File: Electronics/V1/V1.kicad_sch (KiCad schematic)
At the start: 2 parts, among them U1 ADPD144RI, U3 XIAO-ESP32-C3

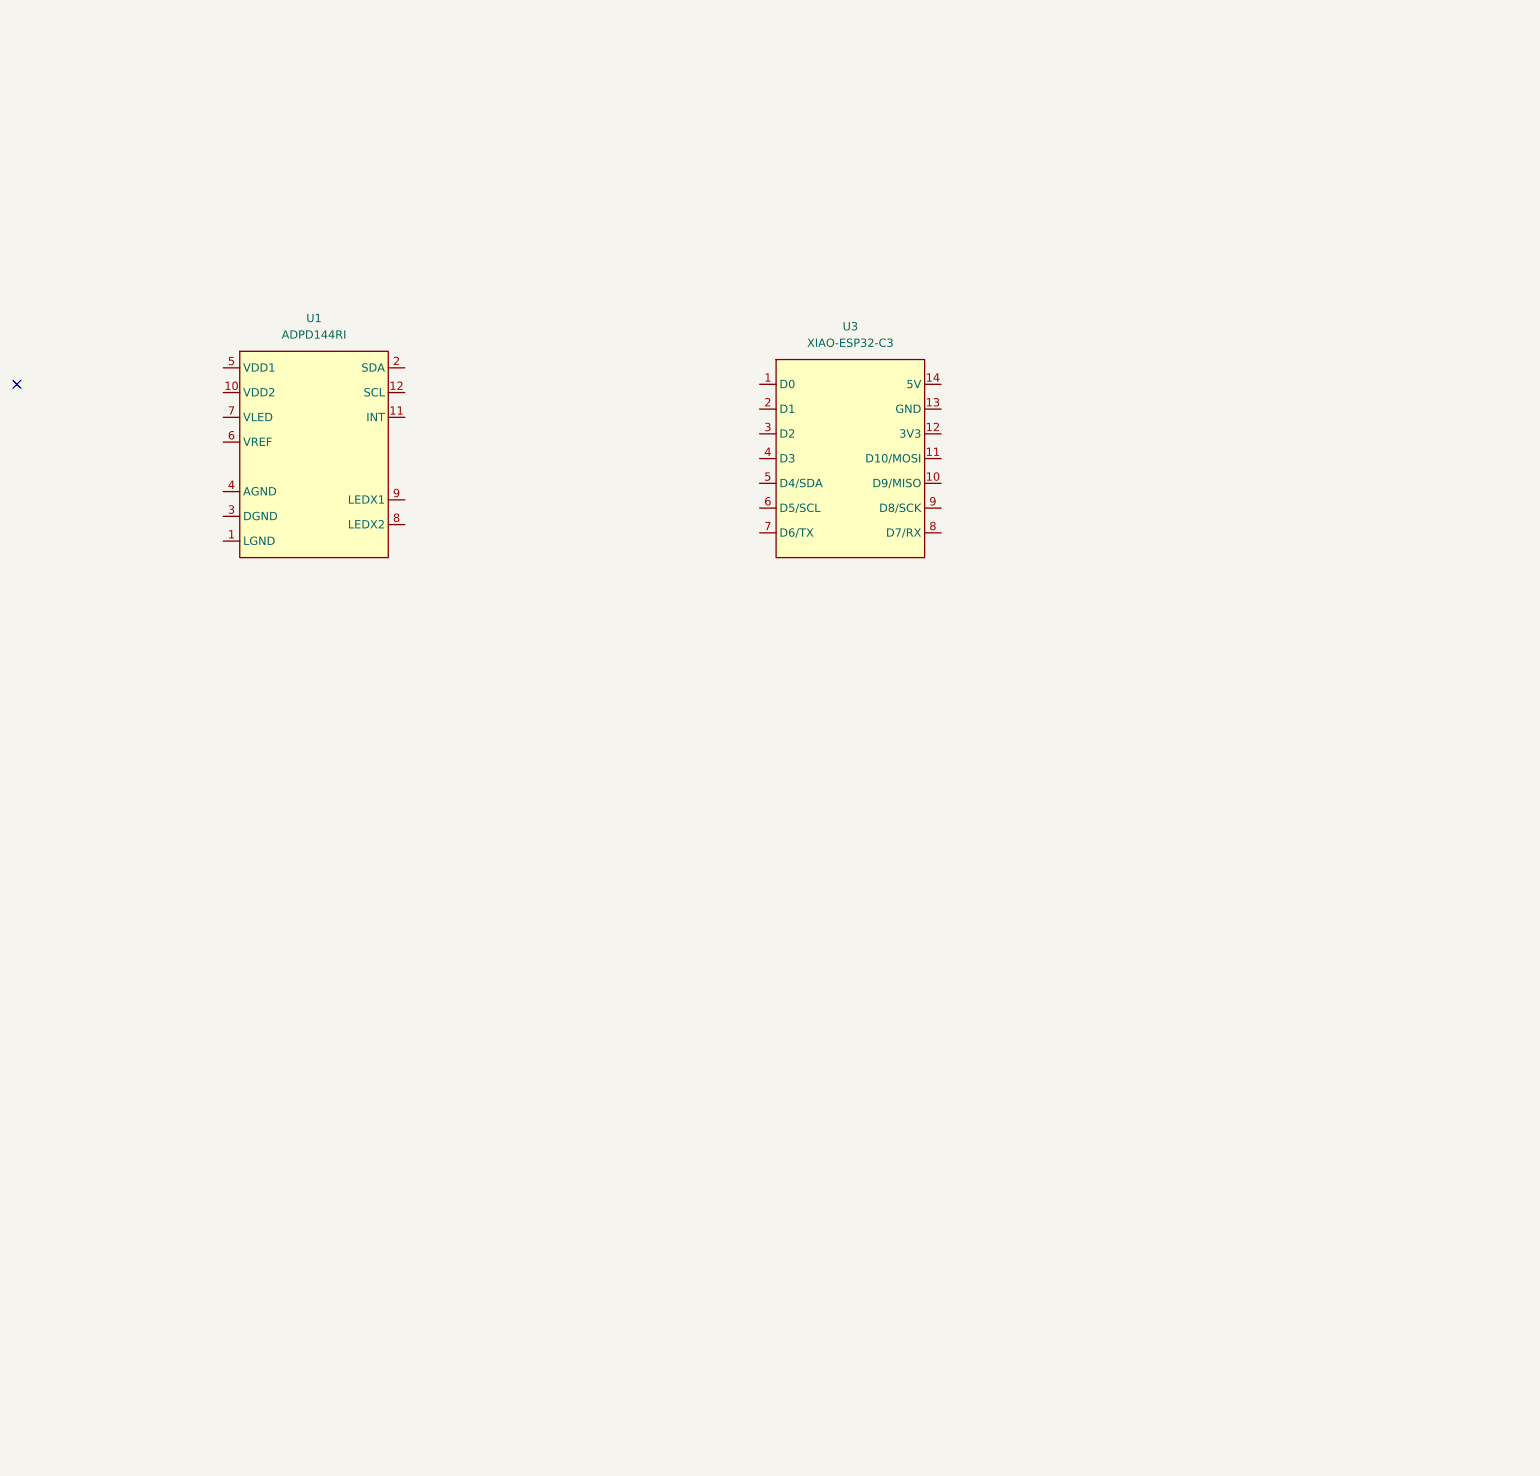
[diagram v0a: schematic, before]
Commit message: Added more symbols
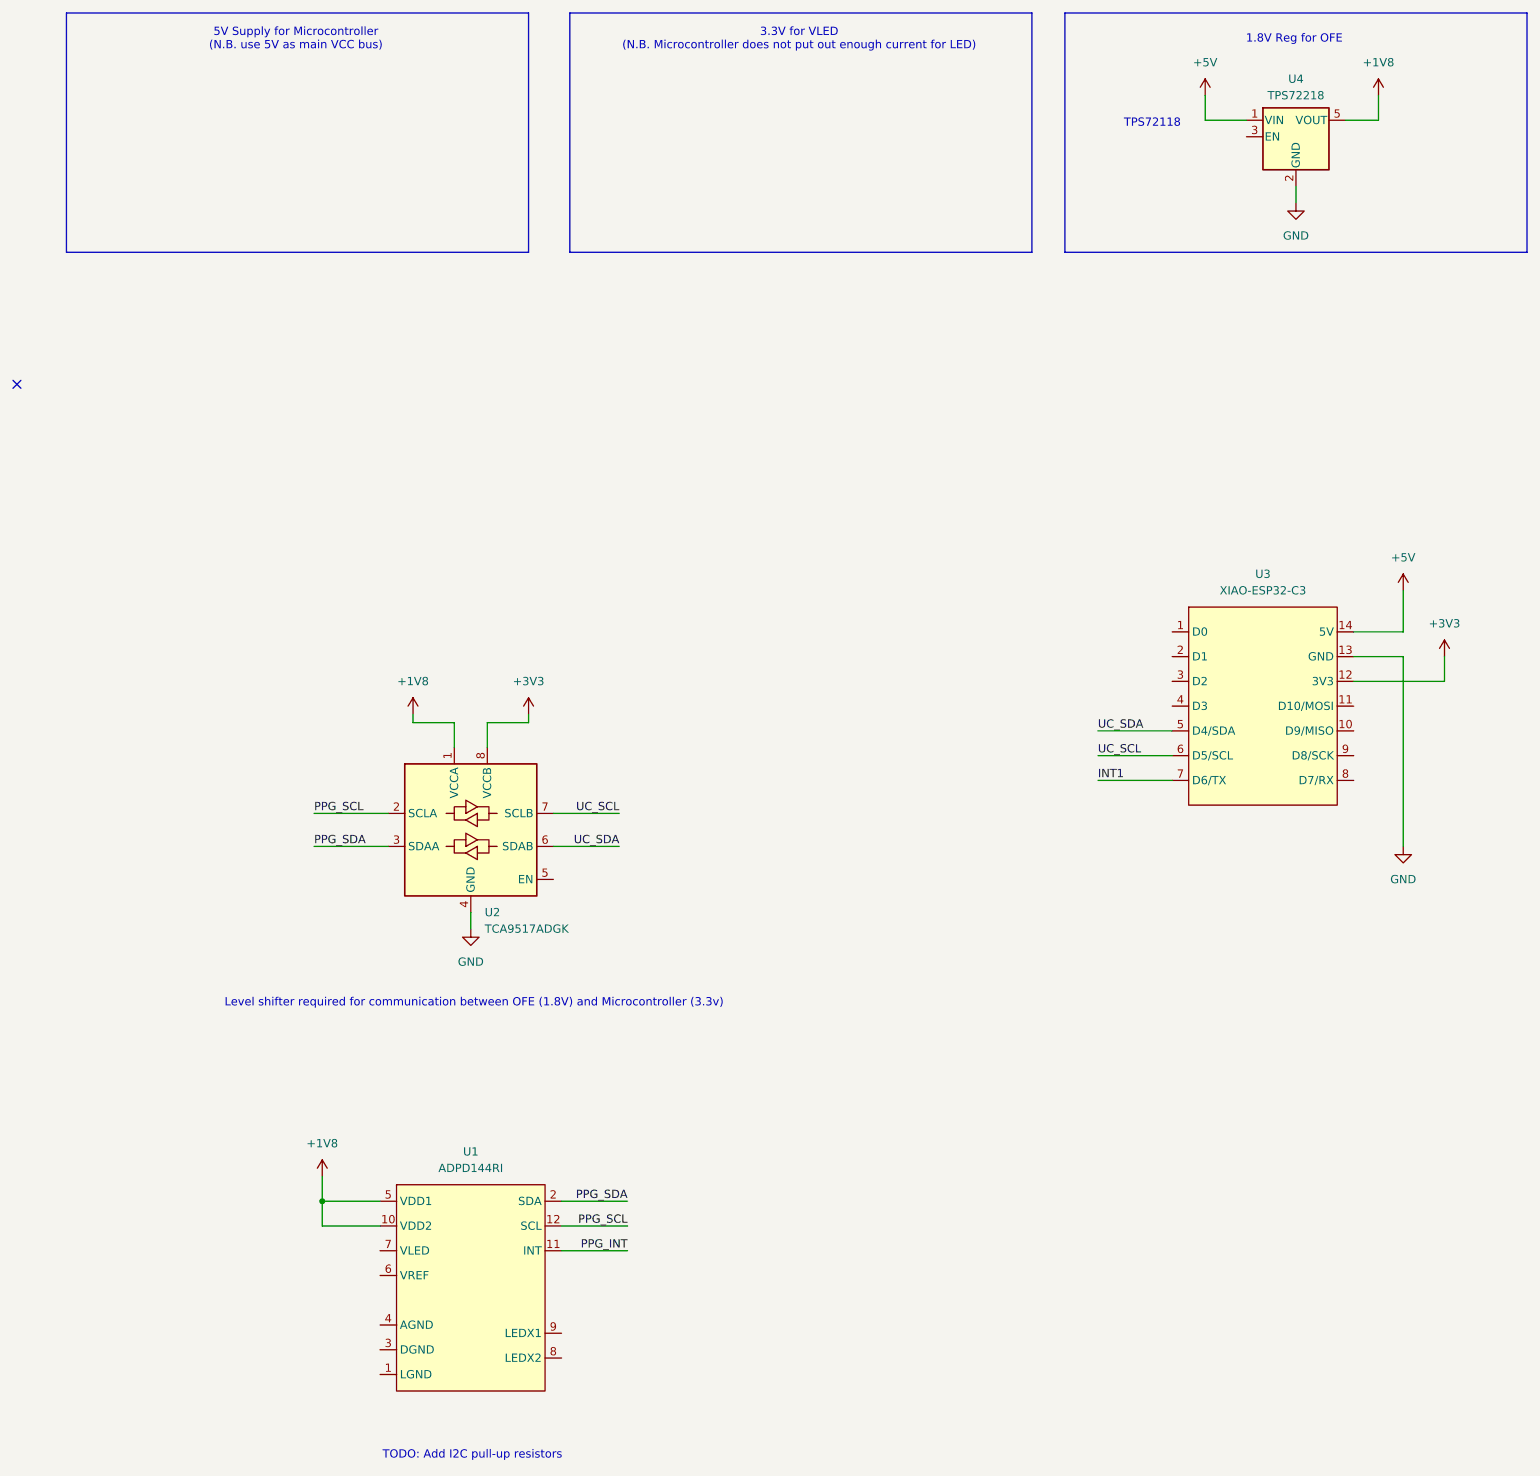
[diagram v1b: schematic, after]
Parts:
- added U2: TCA9517ADGK, Package_SO:VSSOP-8_3x3mm_P0.65mm, symbol Logic_LevelTranslator:TCA9517ADGK
- added U4: TPS72218, Package_TO_SOT_SMD:SOT-23-5, symbol Regulator_Linear:TPS72218
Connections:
- net +1V8: now reaches U1.10 (VDD2)
- net +1V8: now also U1.5 (VDD1), U2.1 (VCCA), U4.5 (VOUT)
- net PPG_INT: now reaches U1.11 (INT)
- net PPG_SCL: now reaches U1.12 (SCL)
- net PPG_SCL: now also U2.2 (SCLA)
- net PPG_SDA: now reaches U1.2 (SDA)
- net PPG_SDA: now also U2.3 (SDAA)
- net +3V3: now reaches U3.12 (3V3)
- net +3V3: now also U2.8 (VCCB)
- net GND: now reaches U3.13 (GND)
- net GND: now also U2.4 (GND), U4.2 (GND)
- net +5V: now reaches U3.14 (5V)
- net +5V: now also U4.1 (VIN)
- net UC_SDA: now reaches U3.5 (D4/SDA)
- net UC_SDA: now also U2.6 (SDAB)
- net UC_SCL: now reaches U3.6 (D5/SCL)
- net UC_SCL: now also U2.7 (SCLB)
- net INT1: now reaches U3.7 (D6/TX)
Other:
- note added: "1.8V Reg for OFE"
- note added: "3.3V for VLED (N.B. Microcontroller does not put out enough current for LED)"
- note added: "5V Supply for Microcontroller (N.B. use 5V as main VCC bus)"
- note added: "Level shifter required for communication between OFE (1.8V) and Microcontroller (3.3v)"
- note added: "TODO: Add I2C pull-up resistors"
- note added: "TPS72118"
- moved on the sheet: U1, U3

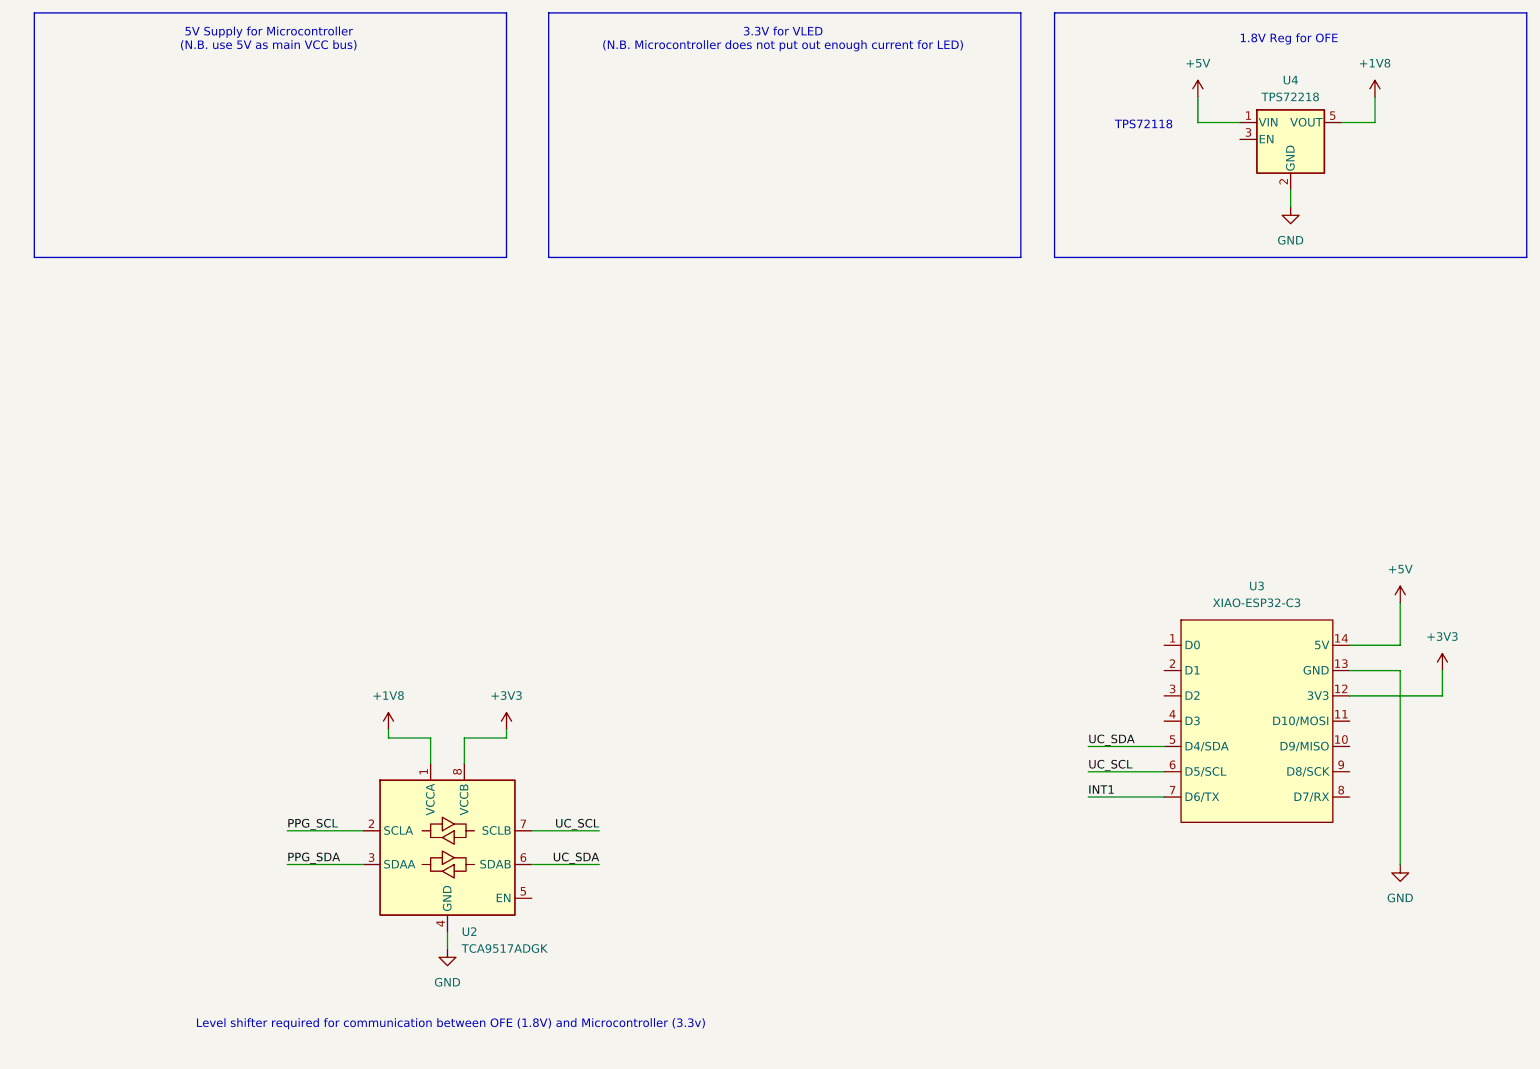
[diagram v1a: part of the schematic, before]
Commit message: added capacitors and pull-up resistors
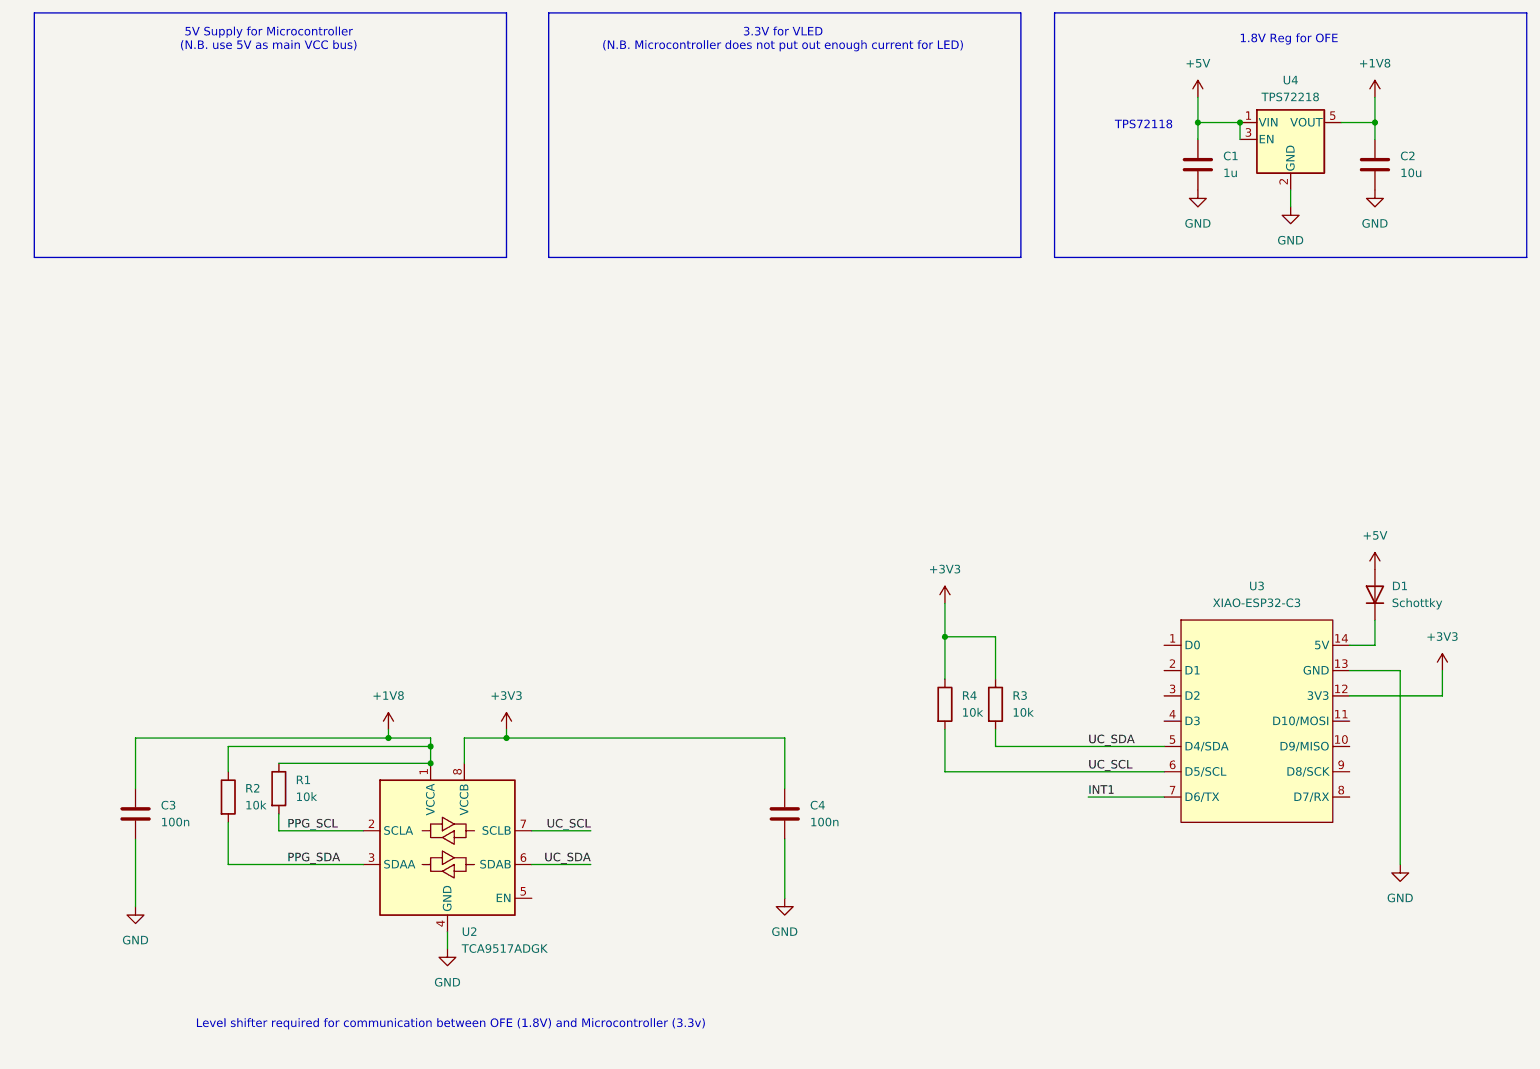
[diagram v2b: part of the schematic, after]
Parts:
- added C1: 1u, Capacitor_SMD:C_0603_1608Metric_Pad1.08x0.95mm_HandSolder, symbol Device:C
- added C2: 10u, Capacitor_SMD:C_0603_1608Metric_Pad1.08x0.95mm_HandSolder, symbol Device:C
- added C3, C4: 100n, Capacitor_SMD:C_0603_1608Metric_Pad1.08x0.95mm_HandSolder, symbol Device:C
- added D1: Schottky, symbol Device:D
- added R1, R2, R3, R4: 10k, symbol Device:R
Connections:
- net +1V8: now also C2.1, C3.1, R1.1, R2.1
- net +3V3: now also C4.1, R3.1, R4.1
- net +5V: now also U4.3 (EN), C1.1, D1.2 (A); no longer U3.14 (5V)
- net GND: now also C1.2, C2.2, C3.2, C4.2
- net PPG_SCL: now also R1.2
- net PPG_SDA: now also R2.2
- net UC_SCL: now also R4.2
- net UC_SDA: now also R3.2
- new net: D1.1 (K), U3.14 (5V)
